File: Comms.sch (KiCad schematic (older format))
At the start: 48 parts, among them J1 Conn_01x05, J2 USB_B_Micro, J6 DNP, U1 93LCxxB, U2 FT232H, U3 ADM2682E, U4 TPD2E2U06, U5 TPD2E2U06, Y1 12MHz

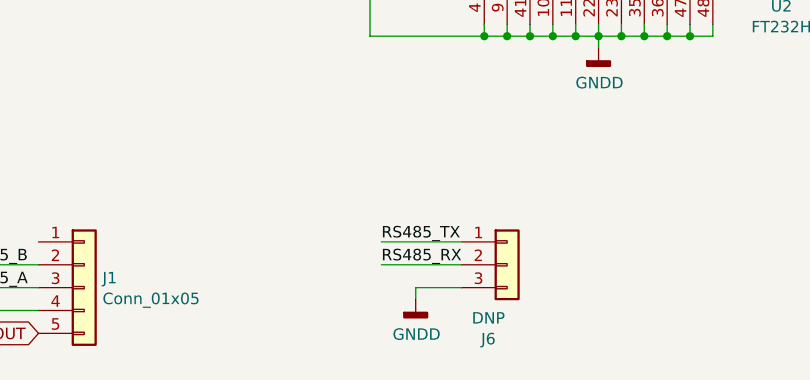
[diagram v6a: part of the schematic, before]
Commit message: Changed connectors to microfit, added fan output
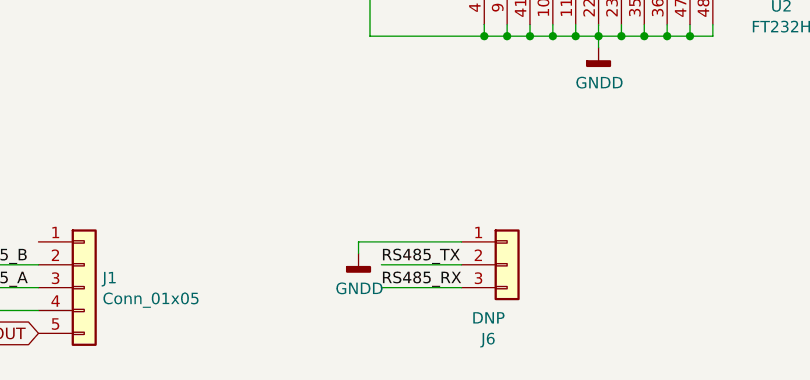
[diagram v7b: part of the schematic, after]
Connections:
- net GNDD: now also J6.1 (Pin_1); no longer J6.3 (Pin_3)
- net RS485_RX: now also J6.3 (Pin_3); no longer J6.2 (Pin_2)
- net RS485_TX: now also J6.2 (Pin_2); no longer J6.1 (Pin_1)

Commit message: add rs485 termination, change to SOT-323 TVS diodes, various OCD
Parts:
- removed U4: TPD2E2U06, Package_TO_SOT_SMD:SOT-553, symbol Power_Protection:TPD2E2U06
- added J8: power-side RS485 debug/expansion, Connector_PinHeader_2.54mm:PinHeader_1x03_P2.54mm_Vertical, symbol Connector_Generic:Conn_01x03
- added R23: 120, Resistor_SMD:R_0603_1608Metric, symbol Device:R_Small
- added U4: TPD2E2U06DCK, Package_TO_SOT_SMD:SOT-323_SC-70, symbol Power_Protection:SP0502BAJT
- J1: value Conn_01x05 -> arm connector
- J6: value DNP -> logic-side RS485 debug/expansion; footprint Connector_PinHeader_2.54mm:PinHeader_1x03_P2.54mm_Vertical -> Connector_PinHeader_2.54mm:PinHeader_1x04_P2.54mm_Vertical; symbol Connector_Generic:Conn_01x03 -> Connector_Generic:Conn_01x04
- U5: value TPD2E2U06 -> TPD2E2U06DCK; footprint Package_TO_SOT_SMD:SOT-553 -> Package_TO_SOT_SMD:SOT-323_SC-70; symbol Power_Protection:TPD2E2U06 -> Power_Protection:SP0502BAJT; D1PN 296-38361-1-ND -> 296-TPD2E2U06DCKRDKR-ND; MPN TPD2E2U06DRLR -> TPD2E2U06DCKR
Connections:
- net DN: now also U5.1 (K); no longer U5.5
- net DP: now also U5.2 (K); no longer U5.3
- net GNDD: now also U5.3 (A); no longer U5.4
- net RS485_A: now also J8.2 (Pin_2), R23.1, U4.2 (K)
- net RS485_B: now also J8.1 (Pin_1), R23.2, U4.1 (K)
- net RS485_DE: now also J6.3 (Pin_3)
- net RS485_RX: now also J6.4 (Pin_4); no longer J6.3 (Pin_3)
- net GNDPWR renamed GND
- net GND: now also J8.3 (Pin_3), U4.3 (A)
- no-connect marks 17 -> 13
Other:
- moved on the sheet: C1, C10, C11, C12, C13, C14, C15, C16, C17, C18, C19, C2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
